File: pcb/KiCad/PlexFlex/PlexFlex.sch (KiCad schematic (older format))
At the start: 2 parts

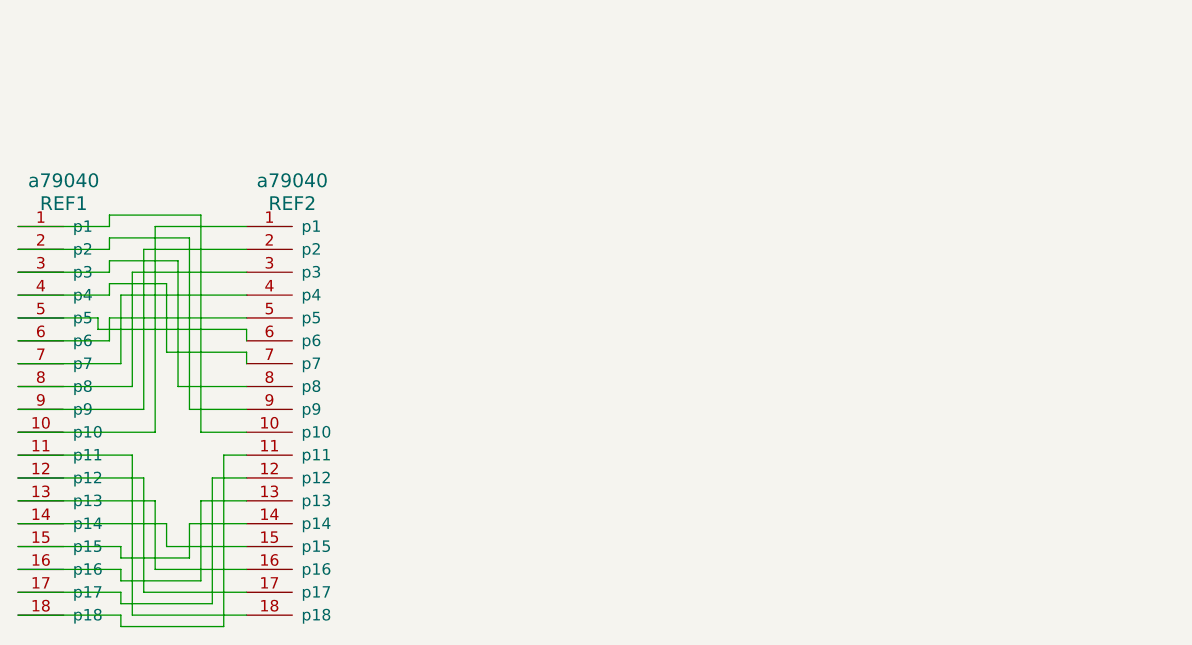
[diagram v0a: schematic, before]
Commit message: Add microphone: knowles_sph1642ht5h-1_revB - Footprint - Schematic - Add to flex cable design
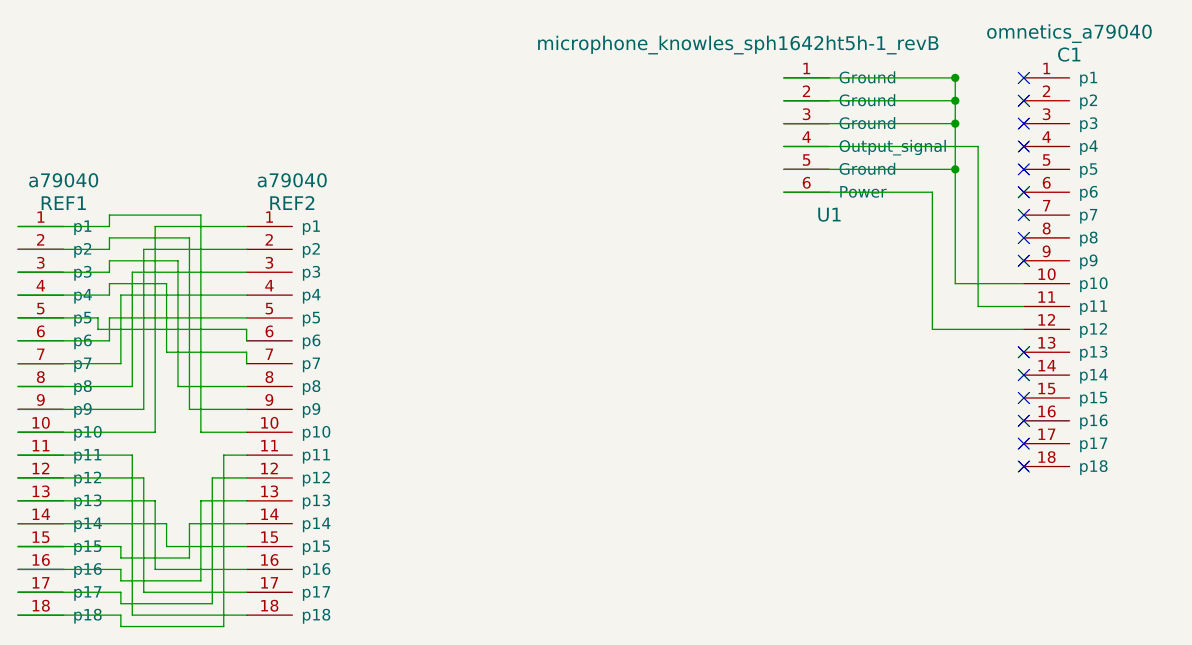
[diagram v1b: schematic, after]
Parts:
- added C1: omnetics_a79040, ugly:a79040, symbol omnetics_a79040
- added U1: microphone_knowles_sph1642ht5h-1_revB, ugly:microphone_knowles_sph1642ht5h-1_revB, symbol microphone_knowles_sph1642ht5h-1_revB
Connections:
- new net: C1.10 (p10), U1.1 (Ground), U1.2 (Ground), U1.3 (Ground), U1.5 (Ground)
- new net: C1.11 (p11), U1.4 (Output_signal)
- new net: C1.12 (p12), U1.6 (Power)
- no-connect marks 0 -> 15
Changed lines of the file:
@@
 	1    0    0    -1
 $EndComp
+$Comp
+L omnetics_a79040 C1
+U 1 1 57A11793
+P 6350 1700
+F 0 "C1" H 6200 1600 60  0000 C CNN
+F 1 "omnetics_a79040" H 6200 1700 60  0000 C CNN
+F 2 "ugly:a79040" H 6200 1600 60  0001 C CNN
+F 3 "" H 6200 1600 60  0000 C CNN
+	1    6350 1700
+	1    0    0    -1
+$EndComp
+$Comp
+L microphone_knowles_sph1642ht5h-1_revB U1
+U 1 1 57A2142B
+P 5150 2500
+F 0 "U1" H 5150 2500 60  0000 C CNN
+F 1 "microphone_knowles_sph1642ht5h-1_revB" H 4750 3250 60  0000 C CNN
+F 2 "ugly:microphone_knowles_sph1642ht5h-1_revB" H 5150 2500 60  0001 C CNN
+F 3 "" H 5150 2500 60  0000 C CNN
+	1    5150 2500
+	1    0    0    -1
+$EndComp
 Wire Wire Line
 	1600 3450 2200 3450
@@
 Wire Wire Line
 	2500 3550 2600 3550
+Wire Wire Line
+	4950 2000 5700 2000
+Connection ~ 5700 1900
+Wire Wire Line
+	5700 2100 4950 2100
+Connection ~ 5700 2000
+Wire Wire Line
+	5700 2300 4950 2300
+Connection ~ 5700 2100
+Wire Wire Line
+	4950 2200 5800 2200
+NoConn ~ 6000 2200
+NoConn ~ 6000 2300
+NoConn ~ 6000 2400
+NoConn ~ 6000 2500
+NoConn ~ 6000 2600
+NoConn ~ 6000 2700
+NoConn ~ 6000 3200
+NoConn ~ 6000 3300
+NoConn ~ 6000 3400
+NoConn ~ 6000 3500
+NoConn ~ 6000 3600
+Wire Wire Line
+	4950 1900 5700 1900
+Connection ~ 5700 2300
+Wire Wire Line
+	5800 2200 5800 2900
+Wire Wire Line
+	5800 2900 6000 2900
+Wire Wire Line
+	4950 2400 5600 2400
+NoConn ~ 6000 1900
+NoConn ~ 6000 2000
+NoConn ~ 6000 2100
+Wire Wire Line
+	6000 2800 5700 2800
+Wire Wire Line
+	5700 2800 5700 1900
+Wire Wire Line
+	5600 2400 5600 3000
+Wire Wire Line
+	5600 3000 6000 3000
+NoConn ~ 6000 3100
 $EndSCHEMATC
